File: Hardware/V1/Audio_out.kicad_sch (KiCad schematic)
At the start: 30 parts, among them J0 0, J1 SJ2-3514A-SMT-TR, J2 0, Q1 BC817-25-QVL

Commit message: motherboard update
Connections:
- net VCC_Audio: now also BZ1.1 (+), D1.1 (K); no longer R8.2
- net at BZ1.2 (-), D1.2 (A): now also R8.2; no longer Q1.3 (C)
- new net: Q1.3 (C), R8.1
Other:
- moved on the sheet: BZ1, D1, R8
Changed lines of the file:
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@@
 	)
 	(junction
-		(at 48.26 29.21)
+		(at 48.26 24.13)
 		(diameter 0)
 		(color 0 0 0 0)
@@
 	)
 	(junction
-		(at 58.42 90.17)
+		(at 48.26 34.29)
 		(diameter 0)
 		(color 0 0 0 0)
 	)
 	(junction
-		(at 60.96 170.18)
+		(at 58.42 90.17)
 		(diameter 0)
 		(color 0 0 0 0)
 	)
 	(junction
-		(at 91.44 157.48)
+		(at 60.96 170.18)
 		(diameter 0)
 		(color 0 0 0 0)
 	)
 	(junction
-		(at 50.8 152.4)
+		(at 91.44 157.48)
 		(diameter 0)
 		(color 0 0 0 0)
 	)
 	(junction
-		(at 48.26 39.37)
+		(at 50.8 152.4)
 		(diameter 0)
 		(color 0 0 0 0)
@@
 	(wire
 		(pts
-			(xy 48.26 19.05) (xy 48.26 21.59)
+			(xy 48.26 19.05) (xy 48.26 24.13)
 		)
 		(stroke
@@
 	(wire
 		(pts
-			(xy 45.72 29.21) (xy 48.26 29.21)
+			(xy 45.72 24.13) (xy 48.26 24.13)
 		)
 		(stroke
@@
 	(wire
 		(pts
-			(xy 48.26 39.37) (xy 48.26 40.64)
-		)
-		(stroke
-			(width 0)
-			(type default)
-		)
-	)
-	(wire
-		(pts
 			(xy 49.53 90.17) (xy 58.42 90.17)
 		)
@@
 	(wire
 		(pts
-			(xy 45.72 36.83) (xy 45.72 39.37)
-		)
-		(stroke
-			(width 0)
-			(type default)
-		)
-	)
-	(wire
-		(pts
-			(xy 48.26 26.67) (xy 48.26 29.21)
+			(xy 45.72 31.75) (xy 45.72 34.29)
 		)
 		(stroke
@@
 	(wire
 		(pts
-			(xy 48.26 29.21) (xy 48.26 31.75)
+			(xy 48.26 24.13) (xy 48.26 26.67)
 		)
 		(stroke
@@
 	(wire
 		(pts
-			(xy 45.72 39.37) (xy 48.26 39.37)
+			(xy 45.72 34.29) (xy 48.26 34.29)
 		)
 		(stroke
@@
 	(wire
 		(pts
+			(xy 48.26 39.37) (xy 48.26 40.64)
+		)
+		(stroke
+			(width 0)
+			(type default)
+		)
+	)
+	(wire
+		(pts
 			(xy 58.42 113.03) (xy 62.23 113.03)
 		)
@@
 	(wire
 		(pts
-			(xy 45.72 31.75) (xy 45.72 29.21)
+			(xy 45.72 26.67) (xy 45.72 24.13)
 		)
 		(stroke
@@
 	(wire
 		(pts
-			(xy 48.26 36.83) (xy 48.26 39.37)
+			(xy 48.26 31.75) (xy 48.26 34.29)
 		)
 		(stroke
@@
 	(symbol
 		(lib_id "Device:Buzzer")
-		(at 50.8 34.29 0)
+		(at 50.8 29.21 0)
 		(unit 1)
 		(exclude_from_sim no)
@@
 		(fields_autoplaced yes)
 		(property "Reference" "BZ1"
-			(at 54.61 33.0199 0)
+			(at 54.61 27.9399 0)
 			(effects
 				(font
@@
 		)
 		(property "Value" "Buzzer"
-			(at 54.61 35.5599 0)
+			(at 54.61 30.4799 0)
 			(effects
 				(font
@@
 		)
 		(property "Footprint" "CMT052575SMTTR"
-			(at 50.165 31.75 90)
+			(at 50.165 26.67 90)
 			(effects
 				(font
@@
 		)
 		(property "Datasheet" "https://datasheet.datasheetarchive.com/originals/distributors/Datasheets_SAMA/202edec26f194914f30bb21e54dbec55.pdf"
-			(at 50.165 31.75 90)
+			(at 50.165 26.67 90)
 			(effects
 				(font
@@
 		)
 		(property "Description" "Buzzer, polarized"
-			(at 50.8 34.29 0)
+			(at 50.8 29.21 0)
 			(effects
 				(font
@@
 	(symbol
 		(lib_id "Device:D_Small")
-		(at 45.72 34.29 90)
+		(at 45.72 29.21 90)
 		(mirror x)
 		(unit 1)
@@
 		(dnp no)
 		(property "Reference" "D1"
-			(at 43.18 33.0199 90)
+			(at 43.18 27.9399 90)
 			(effects
 				(font
@@
 		)
 		(property "Value" "FM4004-W"
-			(at 43.18 35.5599 90)
+			(at 43.18 30.4799 90)
 			(effects
 				(font
@@
 		)
 		(property "Footprint" "DIONM5025X231N"
-			(at 45.72 34.29 90)
+			(at 45.72 29.21 90)
 			(effects
 				(font
@@
 		)
 		(property "Datasheet" "~"
-			(at 45.72 34.29 90)
+			(at 45.72 29.21 90)
 			(effects
 				(font
@@
 		)
 		(property "Description" "Diode, small symbol"
-			(at 45.72 34.29 0)
+			(at 45.72 29.21 0)
 			(effects
 				(font
@@
 		)
 		(property "Height" "2.31"
-			(at 443.18 45.72 0)
+			(at 443.18 40.64 0)
 			(effects
 				(font
@@
 		)
 		(property "Mouser Part Number" "583-FM4004"
-			(at 543.18 45.72 0)
+			(at 543.18 40.64 0)
 			(effects
 				(font
@@
 		)
 		(property "Mouser Price/Stock" "https://www.mouser.co.uk/ProductDetail/Rectron/FM4004-W?qs=Iw9Ubr57Px3IHNH1bE4l9w%3D%3D"
-			(at 643.18 45.72 0)
+			(at 643.18 40.64 0)
 			(effects
 				(font
@@
 		)
 		(property "Manufacturer_Name" "Rectron"
-			(at 743.18 45.72 0)
+			(at 743.18 40.64 0)
 			(effects
 				(font
@@
 		)
 		(property "Manufacturer_Part_Number" "FM4004-W"
-			(at 843.18 45.72 0)
+			(at 843.18 40.64 0)
 			(effects
 				(font
@@
 		)
 		(property "Sim.Device" "D"
-			(at 45.72 34.29 0)
+			(at 45.72 29.21 0)
 			(effects
 				(font
@@
 		)
 		(property "Sim.Pins" "1=K 2=A"
-			(at 45.72 34.29 0)
+			(at 45.72 29.21 0)
 			(effects
 				(font
@@
 	(symbol
 		(lib_id "Device:R_Small")
-		(at 48.26 24.13 180)
+		(at 48.26 36.83 180)
 		(unit 1)
 		(exclude_from_sim no)
@@
 		(fields_autoplaced yes)
 		(property "Reference" "R8"
-			(at 50.8 22.8599 0)
+			(at 50.8 35.5599 0)
 			(effects
 				(font
@@
 		)
 		(property "Value" "220"
-			(at 50.8 25.3999 0)
+			(at 50.8 38.0999 0)
 			(effects
 				(font
@@
 		)
 		(property "Footprint" "Resistor_SMD:R_0603_1608Metric"
-			(at 48.26 24.13 0)
+			(at 48.26 36.83 0)
 			(effects
 				(font
@@
 		)
 		(property "Datasheet" "~"
-			(at 48.26 24.13 0)
+			(at 48.26 36.83 0)
 			(effects
 				(font
@@
 		)
 		(property "Description" "Resistor, small symbol"
-			(at 48.26 24.13 0)
+			(at 48.26 36.83 0)
 			(effects
 				(font

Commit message: added keys
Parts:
- BZ1: footprint CMT052575SMTTR -> SamacSys_Parts:CMT052575SMTTR
- D1: footprint DIONM5025X231N -> SamacSys_Parts:DIONM5025X231N
- J1: footprint SJ23514ASMTTR -> SamacSys_Parts:SJ23514ASMTTR
- Q1: footprint SOT95P230X110-3N -> SamacSys_Parts:SOT95P230X110-3N
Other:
- moved on the sheet: BZ1, D1
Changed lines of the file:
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@@
 	(paper "A4")
 	(junction
+		(at 48.26 33.02)
+		(diameter 0)
+		(color 0 0 0 0)
+	)
+	(junction
 		(at 60.96 175.26)
 		(diameter 0)
@@
 	)
 	(junction
-		(at 48.26 24.13)
+		(at 48.26 22.86)
 		(diameter 0)
 		(color 0 0 0 0)
@@
 	)
 	(junction
-		(at 48.26 34.29)
-		(diameter 0)
-		(color 0 0 0 0)
-	)
-	(junction
 		(at 58.42 90.17)
 		(diameter 0)
@@
 	(wire
 		(pts
-			(xy 48.26 19.05) (xy 48.26 24.13)
+			(xy 48.26 19.05) (xy 48.26 22.86)
 		)
 		(stroke
@@
 	(wire
 		(pts
-			(xy 45.72 24.13) (xy 48.26 24.13)
+			(xy 45.72 22.86) (xy 48.26 22.86)
 		)
 		(stroke
@@
 	(wire
 		(pts
-			(xy 45.72 31.75) (xy 45.72 34.29)
+			(xy 45.72 30.48) (xy 45.72 33.02)
 		)
 		(stroke
@@
 	(wire
 		(pts
-			(xy 48.26 24.13) (xy 48.26 26.67)
+			(xy 48.26 22.86) (xy 48.26 25.4)
 		)
 		(stroke
@@
 	(wire
 		(pts
-			(xy 45.72 34.29) (xy 48.26 34.29)
+			(xy 45.72 33.02) (xy 48.26 33.02)
 		)
 		(stroke
@@
 	(wire
 		(pts
-			(xy 45.72 26.67) (xy 45.72 24.13)
+			(xy 45.72 25.4) (xy 45.72 22.86)
 		)
 		(stroke
@@
 	(wire
 		(pts
-			(xy 48.26 31.75) (xy 48.26 34.29)
+			(xy 48.26 33.02) (xy 48.26 34.29)
+		)
+		(stroke
+			(width 0)
+			(type default)
+		)
+	)
+	(wire
+		(pts
+			(xy 48.26 30.48) (xy 48.26 33.02)
 		)
 		(stroke
@@
 	(symbol
 		(lib_id "Device:Buzzer")
-		(at 50.8 29.21 0)
+		(at 50.8 27.94 0)
 		(unit 1)
 		(exclude_from_sim no)
@@
 		(fields_autoplaced yes)
 		(property "Reference" "BZ1"
-			(at 54.61 27.9399 0)
+			(at 54.61 26.6699 0)
 			(effects
 				(font
@@
 		)
 		(property "Value" "Buzzer"
-			(at 54.61 30.4799 0)
+			(at 54.61 29.2099 0)
 			(effects
 				(font
@@
 			)
 		)
-		(property "Footprint" "CMT052575SMTTR"
-			(at 50.165 26.67 90)
+		(property "Footprint" "SamacSys_Parts:CMT052575SMTTR"
+			(at 50.165 25.4 90)
 			(effects
 				(font
@@
 		)
 		(property "Datasheet" "https://datasheet.datasheetarchive.com/originals/distributors/Datasheets_SAMA/202edec26f194914f30bb21e54dbec55.pdf"
-			(at 50.165 26.67 90)
+			(at 50.165 25.4 90)
 			(effects
 				(font
@@
 		)
 		(property "Description" "Buzzer, polarized"
-			(at 50.8 29.21 0)
+			(at 50.8 27.94 0)
 			(effects
 				(font
@@
 			)
 		)
-		(property "Footprint" "SJ23514ASMTTR"
+		(property "Footprint" "SamacSys_Parts:SJ23514ASMTTR"
 			(at 134.62 192.71 0)
 			(effects
@@
 	(symbol
 		(lib_id "Device:D_Small")
-		(at 45.72 29.21 90)
+		(at 45.72 27.94 90)
 		(mirror x)
 		(unit 1)
@@
 		(dnp no)
 		(property "Reference" "D1"
-			(at 43.18 27.9399 90)
+			(at 43.18 26.6699 90)
 			(effects
 				(font
@@
 		)
 		(property "Value" "FM4004-W"
-			(at 43.18 30.4799 90)
+			(at 43.18 29.2099 90)
 			(effects
 				(font
@@
 			)
 		)
-		(property "Footprint" "DIONM5025X231N"
-			(at 45.72 29.21 90)
+		(property "Footprint" "SamacSys_Parts:DIONM5025X231N"
+			(at 45.72 27.94 90)
 			(effects
 				(font
@@
 		)
 		(property "Datasheet" "~"
-			(at 45.72 29.21 90)
+			(at 45.72 27.94 90)
 			(effects
 				(font
@@
 		)
 		(property "Description" "Diode, small symbol"
-			(at 45.72 29.21 0)
+			(at 45.72 27.94 0)
 			(effects
 				(font
@@
 		)
 		(property "Height" "2.31"
-			(at 443.18 40.64 0)
+			(at 443.18 39.37 0)
 			(effects
 				(font
@@
 		)
 		(property "Mouser Part Number" "583-FM4004"
-			(at 543.18 40.64 0)
+			(at 543.18 39.37 0)
 			(effects
 				(font
@@
 		)
 		(property "Mouser Price/Stock" "https://www.mouser.co.uk/ProductDetail/Rectron/FM4004-W?qs=Iw9Ubr57Px3IHNH1bE4l9w%3D%3D"
-			(at 643.18 40.64 0)
+			(at 643.18 39.37 0)
 			(effects
 				(font
@@
 		)
 		(property "Manufacturer_Name" "Rectron"
-			(at 743.18 40.64 0)
+			(at 743.18 39.37 0)
 			(effects
 				(font
@@
 		)
 		(property "Manufacturer_Part_Number" "FM4004-W"
-			(at 843.18 40.64 0)
+			(at 843.18 39.37 0)
 			(effects
 				(font
@@
 		)
 		(property "Sim.Device" "D"
-			(at 45.72 29.21 0)
+			(at 45.72 27.94 0)
 			(effects
 				(font
@@
 		)
 		(property "Sim.Pins" "1=K 2=A"
-			(at 45.72 29.21 0)
+			(at 45.72 27.94 0)
 			(effects
 				(font
@@
 			)
 		)
-		(property "Footprint" "SOT95P230X110-3N"
+		(property "Footprint" "SamacSys_Parts:SOT95P230X110-3N"
 			(at 52.07 149.53 0)
 			(effects

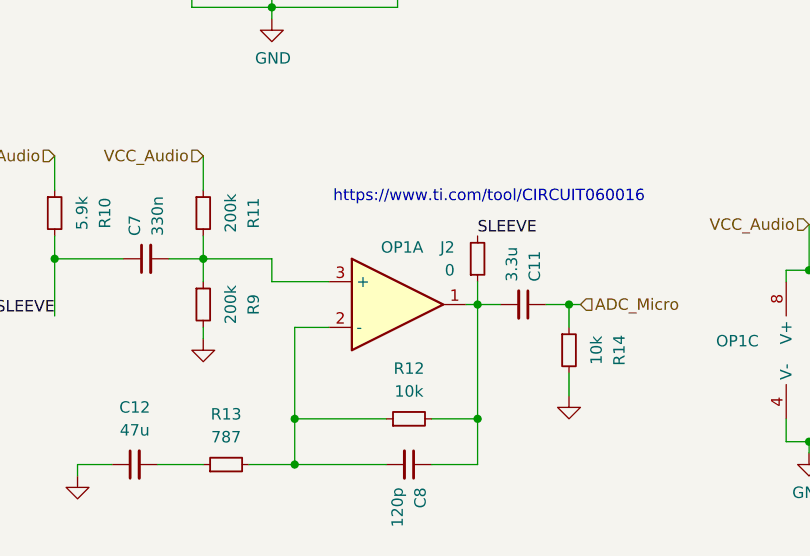
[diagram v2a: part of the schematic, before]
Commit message: refined footprint
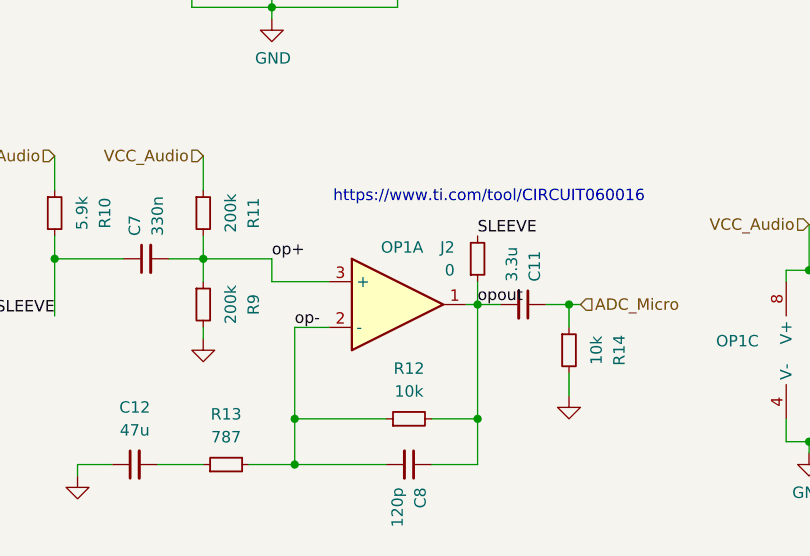
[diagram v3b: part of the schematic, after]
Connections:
- net op+: now reaches C7.2, OP1.3 (+), R11.2, R9.1
- net op-: now reaches C8.2, OP1.2 (-), R12.1, R13.2
- net opout: now reaches C11.2, C8.1, J2.1, OP1.1, R12.2
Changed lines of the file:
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@@
+		)
+	)
+	(label "op+"
+		(at 58.42 152.4 0)
+		(fields_autoplaced yes)
+		(effects
+			(font
+				(size 1.27 1.27)
+			)
+			(justify left bottom)
+		)
+	)
+	(label "op-"
+		(at 60.96 160.02 0)
+		(fields_autoplaced yes)
+		(effects
+			(font
+				(size 1.27 1.27)
+			)
+			(justify left bottom)
 		)
 	)
@@
 		(fields_autoplaced yes)
 		(effects
+			(font
+				(size 1.27 1.27)
+			)
+			(justify left bottom)
+		)
+	)
+	(label "opout"
+		(at 81.28 157.48 0)
+		(fields_autoplaced yes)
+		(effects

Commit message: a
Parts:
- removed C12: 47u, Capacitor_SMD:C_1206_3216Metric_Pad1.33x1.80mm_HandSolder, symbol Device:C_Small
- added C10: 47u, Capacitor_SMD:C_1206_3216Metric_Pad1.33x1.80mm_HandSolder, symbol Device:C_Small
- added unit 2 of OP1
- C11, C7, C8: footprint Capacitor_SMD:C_0402_1005Metric -> Capacitor_SMD:C_0805_2012Metric_Pad1.18x1.45mm_HandSolder
- renumbered J2 to J_Mic1
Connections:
- net GND: now also C10.1, OP1.5 (+), OP1.6 (-)
- net at R13.1: now also C10.2
- no-connect marks 0 -> 1
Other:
- moved on the sheet: C11, C3, C4, C5, C6, C8, C9, J1, OP1C, R1, R12, R14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

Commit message: asd
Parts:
- removed C10, C3: 47u, Capacitor_SMD:C_1206_3216Metric_Pad1.33x1.80mm_HandSolder, symbol Device:C_Small
- removed C11: 3.3u, Capacitor_SMD:C_0805_2012Metric_Pad1.18x1.45mm_HandSolder, symbol Device:C_Small
- removed C5: 0.1u, Capacitor_SMD:C_0402_1005Metric, symbol Device:C_Small
- removed C9: 0.1uF, Capacitor_SMD:C_0402_1005Metric_Pad0.74x0.62mm_HandSolder, symbol SymbolsBalloonv4:C
- removed J0, J_Mic1: 0, Resistor_SMD:R_0603_1608Metric, symbol Device:R_Small
- removed J1: SJ2-3514A-SMT-TR, SamacSys_Parts:SJ23514ASMTTR, symbol SamacSys_Parts:SJ2-3514A-SMT-TR
- removed OP1: TLV9002QDRQ1, SamacSys_Parts:SOIC127P600X175-8N, symbol SymbolsBalloonv4:Opamp_Dual
- removed R1, R4: 220, Resistor_SMD:R_0603_1608Metric, symbol Device:R_Small
- removed R10: 5.9k, Resistor_SMD:R_0603_1608Metric_Pad0.98x0.95mm_HandSolder, symbol SymbolsBalloonv4:R_Small
- removed R11, R9: 200k, Resistor_SMD:R_0603_1608Metric_Pad0.98x0.95mm_HandSolder, symbol SymbolsBalloonv4:R_Small
- removed R12, R14: 10k, Resistor_SMD:R_0603_1608Metric_Pad0.98x0.95mm_HandSolder, symbol SymbolsBalloonv4:R_Small
- removed R13: 787, Resistor_SMD:R_0603_1608Metric_Pad0.98x0.95mm_HandSolder, symbol SymbolsBalloonv4:R_Small
- removed R2, R5: 100, Resistor_SMD:R_0603_1608Metric, symbol Device:R_Small
- removed R6: 1.8k, Resistor_SMD:R_0603_1608Metric, symbol Device:R_Small
- added C15, C16, C21: 2u2, SamacSys_Parts:CAPC1608X90N, symbol Device:C_Small
- added C18, C20, C3, C5: 0.1uF, Capacitor_SMD:C_0402_1005Metric_Pad0.74x0.62mm_HandSolder, symbol SymbolsBalloonv4:C
- added C19, C22: 10u, SamacSys_Parts:CAPC1608X50N, symbol Device:C_Small
- added IC3: PCM5101APWR, Package_SO:TSSOP-20_4.4x6.5mm_P0.65mm, symbol Audio:PCM5101A
- added IC4: MIC5528-3.3YMT-TR, SamacSys_Parts:SON40P120X120X60-7N-D, symbol SamacSys_Parts:MIC5528-3.3YMT-TR
- added J1: SJ2-35853B-SMT-TR, SamacSys_Parts:SJ235853BSMTTR, symbol SamacSys_Parts:SJ2-35853B-SMT-TR
- added R1, R2: 470, Resistor_SMD:R_0603_1608Metric_Pad0.98x0.95mm_HandSolder, symbol SymbolsBalloonv4:R_Small
- C4: value 0.1u -> 10u; footprint Capacitor_SMD:C_0402_1005Metric -> SamacSys_Parts:CAPC1608X50N; Height (none) -> 0.5; Manufacturer_Name (none) -> TAIYO YUDEN; Manufacturer_Part_Number (none) -> JMK107ABJ106MA-T; Mouser Part Number (none) -> 963-JMK107ABJ106MA-T; Mouser Price/Stock (none) -> https://www.mouser.co.uk/ProductDetail/Taiyo-Yuden/JMK107AB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
- C6: value 47u -> 2u2; footprint Capacitor_SMD:C_1206_3216Metric_Pad1.33x1.80mm_HandSolder -> SamacSys_Parts:CAPC1608X90N; Height (none) -> 0.9; Manufacturer_Name (none) -> TAIYO YUDEN; Manufacturer_Part_Number (none) -> LMK107BJ225KA-T; Mouser Part Number (none) -> 963-LMK107BJ225KA-T; Mouser Price/Stock (none) -> https://www.mouser.co.uk/ProductDetail/TAIYO-YUDEN/LMK107BJ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
- C7: value 330n -> 2u2; footprint Capacitor_SMD:C_0805_2012Metric_Pad1.18x1.45mm_HandSolder -> SamacSys_Parts:CAPC1608X90N; Height (none) -> 0.9; Manufacturer_Name (none) -> TAIYO YUDEN; Manufacturer_Part_Number (none) -> LMK107BJ225KA-T; Mouser Part Number (none) -> 963-LMK107BJ225KA-T; Mouser Price/Stock (none) -> https://www.mouser.co.uk/ProductDetail/TAIYO-YUDEN/LMK107BJ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
- C8: value 120p -> 2u2; footprint Capacitor_SMD:C_0805_2012Metric_Pad1.18x1.45mm_HandSolder -> SamacSys_Parts:CAPC1608X90N; Height (none) -> 0.9; Manufacturer_Name (none) -> TAIYO YUDEN; Manufacturer_Part_Number (none) -> LMK107BJ225KA-T; Mouser Part Number (none) -> 963-LMK107BJ225KA-T; Mouser Price/Stock (none) -> https://www.mouser.co.uk/ProductDetail/TAIYO-YUDEN/LMK107BJ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
- R3: value 1.8k -> 100k
- R7, R8: value 220 -> ToDo
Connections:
- net SLEEVE is gone; now on net VCC_Audio: C7.1
- net op+ is gone; now on net GND: C7.2
- net op- is gone; now on net GND: C8.2
- net opout is gone; now on net 3V3_A: C8.1
- net Buzzer: now also R3.1
- net GND: now also C15.2, C16.2, C18.1, C19.2, C20.1, C21.2, C22.2, C3.1, C5.1, IC3.10 (DEMP), IC3.11 (FLT), IC3.12 (SCK), IC3.16 (FMT), IC3.19 (DGND), IC3.3 (CPGND), IC3.9 (AGND), IC4.3 (GND), IC4.7 (EP), J1.1 (SLEEVE); no longer R3.1
- net TIP: now also C15.1, J1.2 (TIP), R1.2; no longer R3.2
- net VCC_Audio: now also IC4.4 (EN), IC4.6 (VIN)
- net 3V3_A: now reaches C4.1
- net 3V3_A: now also C18.2, C19.1, C5.2, IC3.1 (CPVDD), IC3.8 (AVDD), IC4.1 (VOUT_1), IC4.2 (VOUT_2)
- net at C6.1: now also IC3.2 (CAPP)
- net RING_1: no longer names the net of C6.2
- net RING_1: now also IC3.4 (CAPM)
- new net: C16.1, C20.2, IC3.5 (VNEG)
- new net: IC3.6 (OUTL), R1.1
- new net: IC3.7 (OUTR), R2.1
- new net 3V3_D: C22.1, C3.2, IC3.17 (XSMT), IC3.20 (DVDD)
- new net Audio_0: IC3.15 (LRCK)
- new net Audio_1: IC3.14 (DIN)
- new net Audio_2: IC3.13 (BCK)
- new net Headphone_connected: J1.10 (TIP_SWITCH), R3.2
- new net RING: C21.1, J1.3 (RING), R2.2
- no-connect marks 1 -> 0
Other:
- note added: "AUDIO"
- note added: "dual function: Headpohne_connected is linked to buzzer -> pulls it down if headphone is connected"
- note removed: "https://embeddedcomputing.com/technology/open-source/development-kits/raspberry-pi-pico-pwm-audio-output-circuit"
- note removed: "https://www.ti.com/tool/CIRCUIT060016"
- moved on the sheet: BZ1, D1, Q1, R7, R8

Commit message: changed to make boom better
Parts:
- C18, C20, C3, C5: value 0.1uF -> 0.1u
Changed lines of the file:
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@@
 			)
 		)
-		(property "Value" "0.1uF"
+		(property "Value" "0.1u"
 			(at 108.585 125.73 0)
 			(effects
@@
 		(fields_autoplaced yes)
 		(property "Reference" "C5"
-			(at 55.245 124.46 0)
+			(at 54.61 124.4599 0)
 			(effects
 				(font
@@
 			)
 		)
-		(property "Value" "0.1uF"
-			(at 55.245 127 0)
+		(property "Value" "0.1u"
+			(at 54.61 126.9999 0)
 			(effects
 				(font
@@
 		(fields_autoplaced yes)
 		(property "Reference" "C18"
-			(at 86.995 105.41 0)
+			(at 87.63 105.4099 0)
 			(effects
 				(font
@@
 			)
 		)
-		(property "Value" "0.1uF"
-			(at 86.995 107.95 0)
+		(property "Value" "0.1u"
+			(at 87.63 107.9499 0)
 			(effects
 				(font
@@
 			)
 		)
-		(property "Value" "0.1uF"
+		(property "Value" "0.1u"
 			(at 107.315 165.1 0)
 			(effects

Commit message: wirked on iS2
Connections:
- net Audio_0 renamed Audio_LRC
- net Audio_1 renamed Audio_DIN
- net Audio_2 renamed Audio_BCK
